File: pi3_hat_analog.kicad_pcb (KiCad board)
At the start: 2 copper layers, 65 x 56 mm, 30 parts, among them J1 1935161, J3 Raspberry_Pi_2_3, J4 SJ1-3533NG, J5 SJ1-3533NG, J6 SJ1-3533NG, J7 SJ1-3533NG, Q1 2N3904BU, U1 MAX31856, U2 MCP3564RT, U3 MAX31856

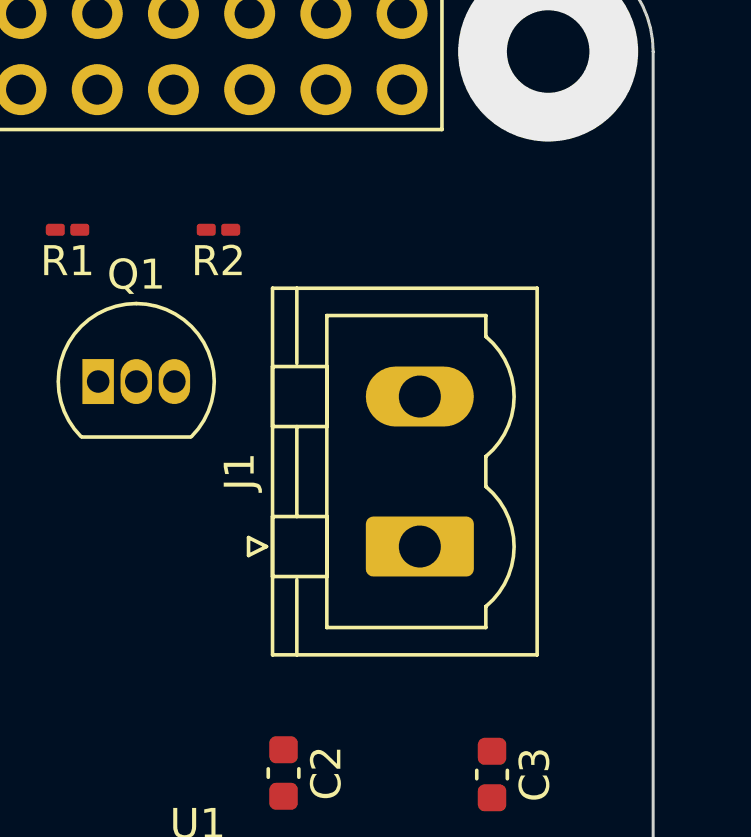
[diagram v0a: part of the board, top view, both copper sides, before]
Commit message: added leds
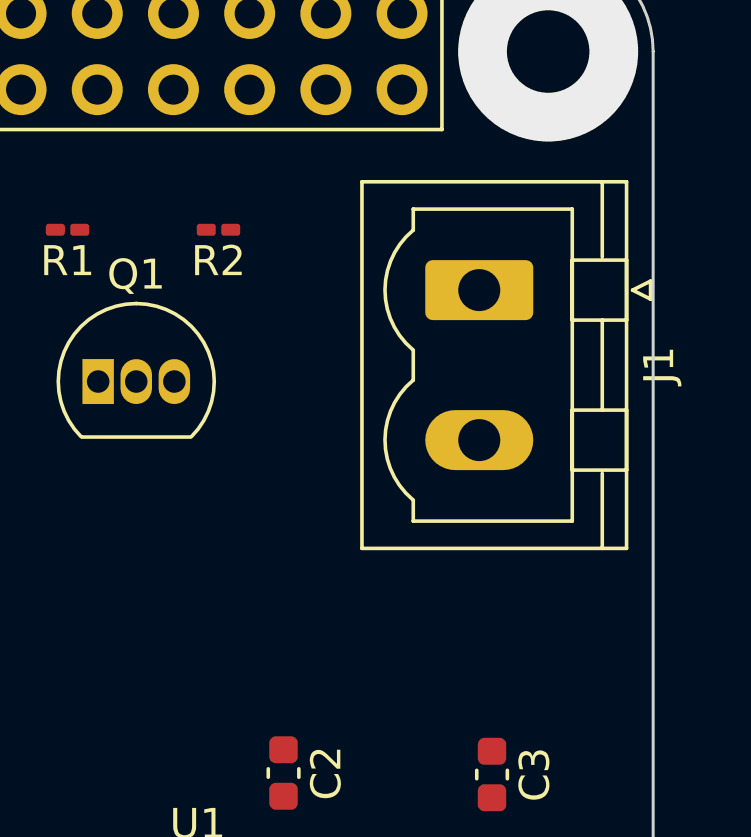
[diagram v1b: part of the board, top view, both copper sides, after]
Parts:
- moved J1 8.77 mm to (105.7, 58.0), turned to -90 degrees
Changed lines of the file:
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@@
   )
   (footprint "Connector_Phoenix_MSTB:PhoenixContact_MSTBVA_2,5_2-G_1x02_P5.00mm_Vertical" (layer "F.Cu")
-    (at 103.7225 66.5 90)
+    (at 105.7035 57.952 -90)
     (descr "Generic Phoenix Contact connector footprint for: MSTBVA_2,5/2-G; number of pins: 02; pin pitch: 5.00mm; Vertical || order number: 1755516 12A || order number: 1924198 16A (HC)")
     (tags "phoenix_contact connector MSTBVA_01x02_G_5.00mm")
@@
     (fp_line (start 0.5 -3.55) (end 0 -2.55) (layer "F.Fab") (width 0.1))
     (fp_line (start -0.5 -3.55) (end 0.5 -3.55) (layer "F.Fab") (width 0.1))
-    (pad "1" thru_hole roundrect (at 0 0 90) (size 2 3.6) (drill 1.4) (layers *.Cu *.Mask) (roundrect_rratio 0.125)
+    (pad "1" thru_hole roundrect (at 0 0 270) (size 2 3.6) (drill 1.4) (layers *.Cu *.Mask) (roundrect_rratio 0.125)
       (net 1 "+3V3") (pinfunction "Pin_1") (pintype "passive"))
-    (pad "2" thru_hole oval (at 5 0 90) (size 2 3.6) (drill 1.4) (layers *.Cu *.Mask)
+    (pad "2" thru_hole oval (at 5 0 270) (size 2 3.6) (drill 1.4) (layers *.Cu *.Mask)
       (net 7 "Net-(J1-Pad2)") (pinfunction "Pin_2") (pintype "passive"))
     (model "${KICAD6_3DMODEL_DIR}/Connector_Phoenix_MSTB.3dshapes/PhoenixContact_MSTBVA_2,5_2-G_1x02_P5.00mm_Vertical.wrl"

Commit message: more placement
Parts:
- added D1: LED, LED_SMD:LED_0603_1608Metric_Pad1.05x0.95mm_HandSolder, F.Cu at (120.7, 54.6)
- added D2: LED, LED_SMD:LED_0603_1608Metric_Pad1.05x0.95mm_HandSolder, F.Cu at (125.0, 57.2)
- added D3: LED, LED_SMD:LED_0603_1608Metric_Pad1.05x0.95mm_HandSolder, F.Cu at (129.4, 57.2)
- added D4: LED, LED_SMD:LED_0603_1608Metric_Pad1.05x0.95mm_HandSolder, F.Cu at (125.0, 59.8)
- added D5: LED, LED_SMD:LED_0603_1608Metric_Pad1.05x0.95mm_HandSolder, F.Cu at (120.7, 57.2)
- added D6: LED, LED_SMD:LED_0603_1608Metric_Pad1.05x0.95mm_HandSolder, F.Cu at (125.0, 54.6)
- added D7: LED, LED_SMD:LED_0603_1608Metric_Pad1.05x0.95mm_HandSolder, F.Cu at (120.7, 62.4)
- added D8: LED, LED_SMD:LED_0603_1608Metric_Pad1.05x0.95mm_HandSolder, F.Cu at (129.4, 54.6)
- added D9: LED, LED_SMD:LED_0603_1608Metric_Pad1.05x0.95mm_HandSolder, F.Cu at (120.7, 59.8)
- added R10: 500, Resistor_SMD:R_0603_1608Metric_Pad0.98x0.95mm_HandSolder, F.Cu at (138.1, 54.6)
- added R15: 500, Resistor_SMD:R_0603_1608Metric_Pad0.98x0.95mm_HandSolder, F.Cu at (129.3, 64.8)
- added R3: 500, Resistor_SMD:R_0603_1608Metric_Pad0.98x0.95mm_HandSolder, F.Cu at (133.8, 54.6)
- added R4: 500, Resistor_SMD:R_0603_1608Metric_Pad0.98x0.95mm_HandSolder, F.Cu at (125.0, 62.3)
- added R5: 500, Resistor_SMD:R_0603_1608Metric_Pad0.98x0.95mm_HandSolder, F.Cu at (133.8, 57.1)
- added R6: 500, Resistor_SMD:R_0603_1608Metric_Pad0.98x0.95mm_HandSolder, F.Cu at (133.7, 59.8)
- added R7: 500, Resistor_SMD:R_0603_1608Metric_Pad0.98x0.95mm_HandSolder, F.Cu at (129.4, 59.8)
- added R8: 500, Resistor_SMD:R_0603_1608Metric_Pad0.98x0.95mm_HandSolder, F.Cu at (138.1, 57.1)
- added R9: 500, Resistor_SMD:R_0603_1608Metric_Pad0.98x0.95mm_HandSolder, F.Cu at (129.4, 62.3)
- added REF**: raspberry pi mounting hole, Library:raspberry pi mounting hole, F.Cu at (108.0, 50.0)
- added REF**: raspberry pi mounting hole, Library:raspberry pi mounting hole, F.Cu at (50.0, 99.0)
- added REF**: raspberry pi mounting hole, Library:raspberry pi mounting hole, F.Cu at (108.0, 99.0)
- added REF**: raspberry pi mounting hole, Library:raspberry pi mounting hole, F.Cu at (50.0, 50.0)
- R1, R11, R12, R13, R14, R2: footprint Resistor_SMD:R_0201_0603Metric_Pad0.64x0.40mm_HandSolder -> Resistor_SMD:R_0603_1608Metric_Pad0.98x0.95mm_HandSolder
- moved R14 19.1 mm to (66.0, 68.6)
- moved C3 17.3 mm to (92.7, 85.1)
- moved C7 15.3 mm to (74.9, 85.1), turned to 90 degrees
- moved C8 14.8 mm to (72.4, 85.1)
- moved C4 12.9 mm to (95.2, 85.0), turned to 90 degrees
- moved R13 12.8 mm to (66.0, 64.8)
- moved C5 8.90 mm to (97.8, 85.0)
- moved C6 8.56 mm to (77.5, 85.1)
- moved C1 7.94 mm to (92.7, 72.4)
- moved C12 6.90 mm to (71.1, 72.4)
- moved R12 6.57 mm to (66.0, 61.0)
- moved U1 3.19 mm to (95.2, 76.2)
- moved C11 2.54 mm to (71.1, 56.1), turned to 180 degrees
- moved C9 2.54 mm to (77.5, 56.1), turned to 0 degrees
- moved C2 2.17 mm to (97.8, 72.4), turned to 180 degrees
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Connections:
- C9 pad 2: GNDREF -> Net-(C9-Pad2)
- U2 pad 19: GNDREF -> Net-(C9-Pad2)
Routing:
- net (no net): vias 4 -> 0

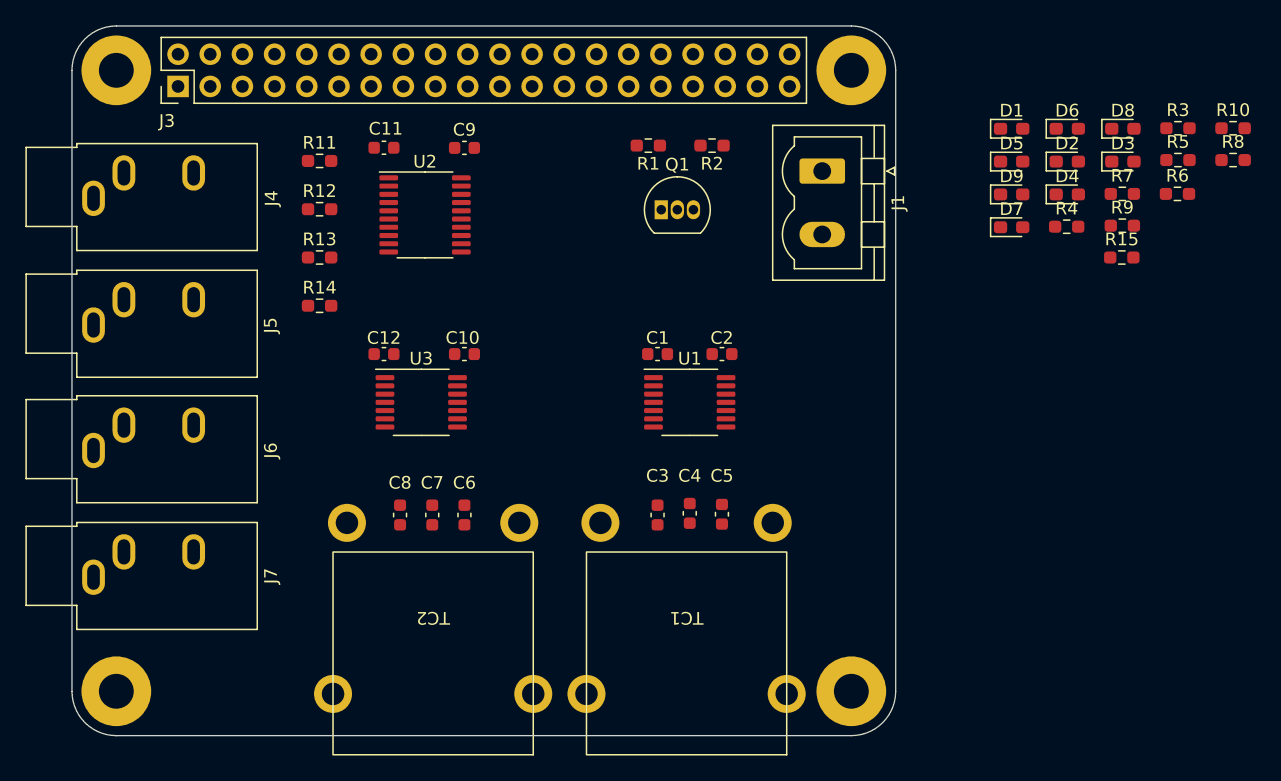
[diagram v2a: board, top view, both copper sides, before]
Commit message: initial component placement complete
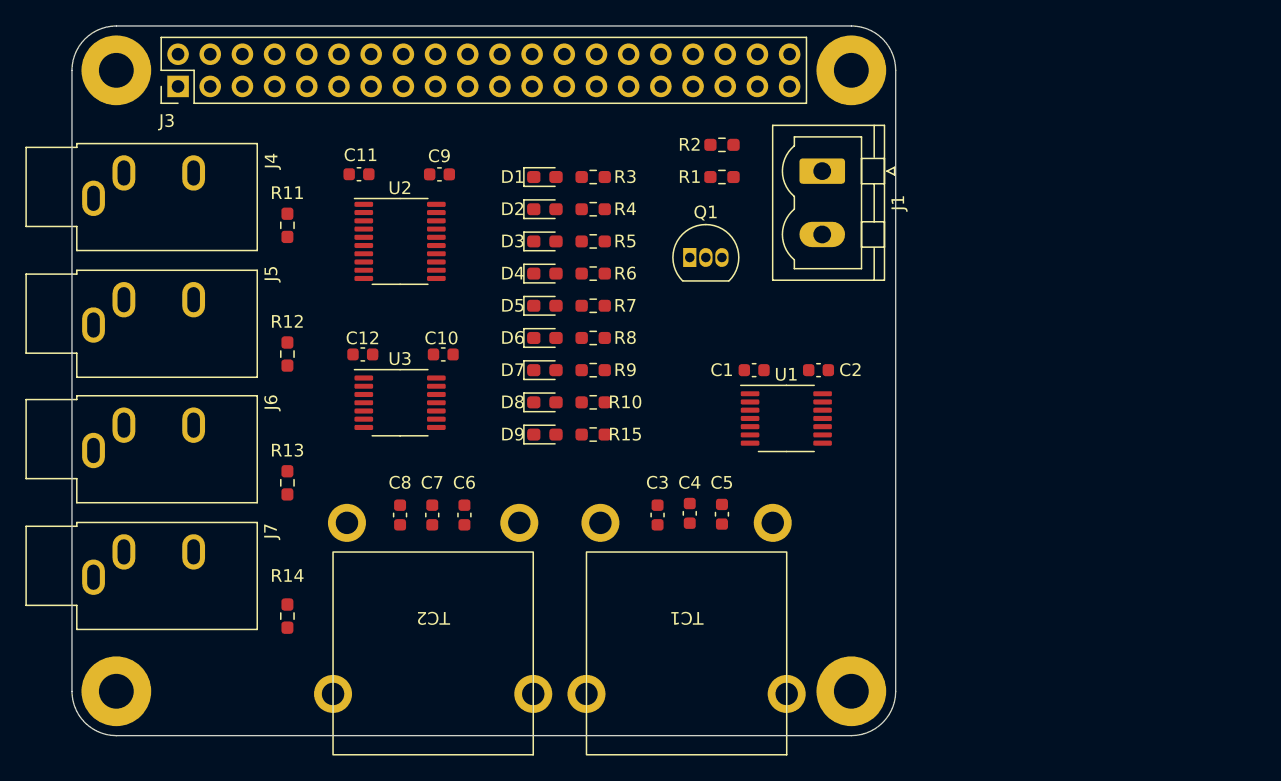
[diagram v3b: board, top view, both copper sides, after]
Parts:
- moved R10 54.9 mm to (87.6, 76.2), turned to 180 degrees
- moved R8 52.4 mm to (87.6, 71.1), turned to 180 degrees
- moved D8 50.5 mm to (83.8, 76.2)
- moved R5 46.6 mm to (87.6, 63.5)
- moved R6 46.5 mm to (87.6, 66.0)
- moved R3 46.3 mm to (87.6, 58.4), turned to 180 degrees
- moved D3 46.0 mm to (83.8, 63.5)
- moved D6 44.4 mm to (83.8, 71.1)
- moved R15 44.0 mm to (87.6, 78.7), turned to 180 degrees
- moved R9 43.3 mm to (87.6, 73.7), turned to 180 degrees
- moved R7 42.7 mm to (87.6, 68.6)
- moved D4 41.7 mm to (83.8, 66.0)
- moved D9 41.4 mm to (83.8, 78.7)
- moved D2 41.4 mm to (83.8, 61.0)
- moved D5 38.5 mm to (83.8, 68.6)
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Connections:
- D1 pad 1: Net-(D1-Pad1) -> GNDREF
- D1 pad 2: +3V3 -> Net-(R3-Pad2)
- D2 pad 1: Net-(D2-Pad1) -> GNDREF
- D2 pad 2: Net-(J3-Pad33) -> Net-(R4-Pad2)
- R3 pad 1: GNDREF -> +3V3
- R3 pad 2: Net-(D1-Pad1) -> Net-(R3-Pad2)
- R4 pad 1: GNDREF -> Net-(J3-Pad33)
- R4 pad 2: Net-(D2-Pad1) -> Net-(R4-Pad2)
- R5 pad 1: Net-(J3-Pad12) -> Net-(D3-Pad2)
- R5 pad 2: Net-(D3-Pad2) -> Net-(J3-Pad12)
- R6 pad 1: Net-(J3-Pad38) -> Net-(D4-Pad2)
- R6 pad 2: Net-(D4-Pad2) -> Net-(J3-Pad38)
- R7 pad 1: Net-(J3-Pad35) -> Net-(D5-Pad2)
- R7 pad 2: Net-(D5-Pad2) -> Net-(J3-Pad35)

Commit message: traces in progress
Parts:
- moved D1 20.8 mm to (101.9, 68.8)
- moved R3 20.8 mm to (105.7, 68.8)
- moved D2 20.6 mm to (101.9, 70.9)
- moved R4 20.6 mm to (105.7, 70.9)
- moved C2 7.62 mm to (105.4, 81.3)
- moved C10 0.62 mm to (75.2, 72.4), turned to 0 degrees
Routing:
- net +3V3: track 0.00 -> 235.7 mm
- net Net-(J3-Pad26): track 0.00 -> 30.7 mm
- net Net-(J3-Pad33): track 0.00 -> 29.5 mm, vias 0 -> 2
- net Net-(J5-PadT): track 0.00 -> 28.0 mm, vias 0 -> 2
- net Net-(C6-Pad2): track 0.00 -> 27.1 mm, vias 0 -> 2
- net Net-(C7-Pad2): track 0.00 -> 21.3 mm
- net Net-(J7-PadT): track 0.00 -> 14.6 mm, vias 0 -> 1
- net Net-(J6-PadT): track 0.00 -> 14.4 mm, vias 0 -> 1
- net Net-(J4-PadT): track 0.00 -> 14.4 mm, vias 0 -> 1
- net Net-(Q1-Pad2): track 0.00 -> 9.79 mm
- net Net-(J1-Pad2): track 0.00 -> 8.67 mm
- net GNDREF: track 0.00 -> 7.63 mm
- net Net-(D9-Pad2): track 0.00 -> 2.02 mm
- net Net-(D8-Pad2): track 0.00 -> 2.02 mm
- net Net-(D7-Pad2): track 0.00 -> 2.02 mm
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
